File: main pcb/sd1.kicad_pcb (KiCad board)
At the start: 2 copper layers, 66.1 x 60 mm, 14 parts

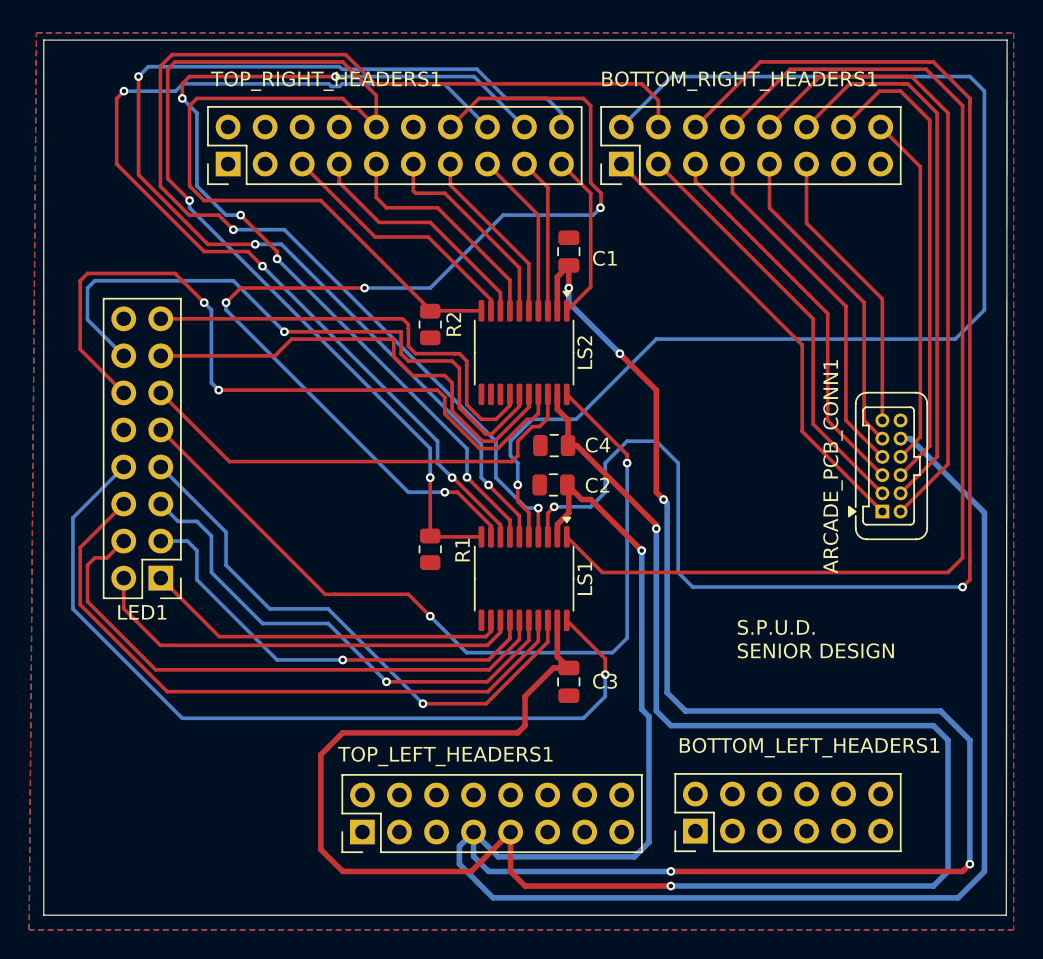
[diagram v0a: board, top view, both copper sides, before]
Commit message: updated main pcb with new connector
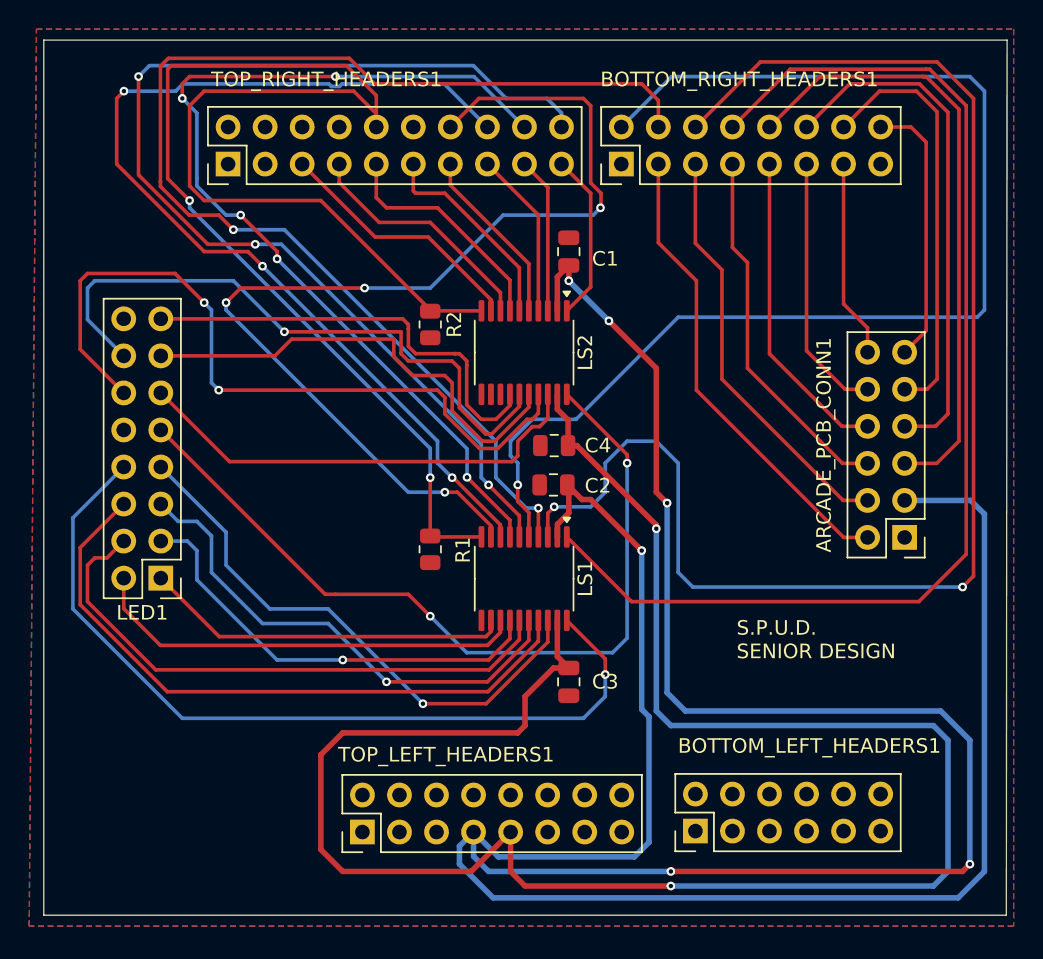
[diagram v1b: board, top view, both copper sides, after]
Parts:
- ARCADE_PCB_CONN1: footprint Connector_Harwin:Harwin_Gecko-G125-FVX1205L0X_2x06_P1.25mm_Vertical -> Connector_PinHeader_2.54mm:PinHeader_2x06_P2.54mm_Vertical
- moved ARCADE_PCB_CONN1 2.34 mm to (174.0, 109.1), turned to 180 degrees
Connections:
- ARCADE_PCB_CONN1 pad 1: ARC1 -> GND
- ARCADE_PCB_CONN1 pad 10: ARC10 -> ARC5
- ARCADE_PCB_CONN1 pad 11: 3.3V -> ARC10
- ARCADE_PCB_CONN1 pad 12: GND -> ARC6
- ARCADE_PCB_CONN1 pad 2: ARC2 -> ARC1
- ARCADE_PCB_CONN1 pad 3: ARC3 -> 3.3V
- ARCADE_PCB_CONN1 pad 4: ARC4 -> ARC2
- ARCADE_PCB_CONN1 pad 5: ARC5 -> ARC7
- ARCADE_PCB_CONN1 pad 6: ARC6 -> ARC3
- ARCADE_PCB_CONN1 pad 7: ARC7 -> ARC8
- ARCADE_PCB_CONN1 pad 8: ARC8 -> ARC4
- BOTTOM_RIGHT_HEADERS1 pad 1: ARC1 -> unconnected-(BOTTOM_RIGHT_HEADERS1-IO-Pad1)
- BOTTOM_RIGHT_HEADERS1 pad 11: ARC6 -> ARC5
- BOTTOM_RIGHT_HEADERS1 pad 13: unconnected-(BOTTOM_RIGHT_HEADERS1-IO-Pad13) -> ARC6
- BOTTOM_RIGHT_HEADERS1 pad 3: ARC2 -> ARC1
- BOTTOM_RIGHT_HEADERS1 pad 5: ARC3 -> ARC2
- BOTTOM_RIGHT_HEADERS1 pad 7: ARC4 -> ARC3
- BOTTOM_RIGHT_HEADERS1 pad 9: ARC5 -> ARC4
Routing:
- net ARC6: track 19.7 -> 13.6 mm
- net ARC10: track 24.3 -> 18.6 mm
- net ARC9: track 32.9 -> 28.9 mm
- net ARC5: track 22.0 -> 18.1 mm
- net ARC4: track 24.3 -> 21.8 mm
- net ARC8: track 38.1 -> 35.7 mm
- net 3.3V: track 219.5 -> 217.4 mm
- net DATA1: track 78.0 -> 80.0 mm
- net ARC3: track 26.6 -> 25.4 mm
- net ARC1: track 31.2 -> 32.5 mm
- net ARC7: track 43.4 -> 42.5 mm
- net OE: track 104.0 -> 104.7 mm

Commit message: update main pcb
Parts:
- LED1: value Conn_02x08_Top_Bottom -> Conn_02x08_Odd_Even
- moved LED1 16.0 mm to (120.5, 96.1), turned to 0 degrees
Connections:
- LED1 pad 10: GND -> A1
- LED1 pad 11: G1 -> A2
- LED1 pad 12: A4 -> A3
- LED1 pad 13: A1 -> Clock
- LED1 pad 14: A3 -> LATCH
- LED1 pad 15: LATCH -> BLANK
- LED1 pad 2: B0 -> G0
- LED1 pad 3: R1 -> B0
- LED1 pad 4: B1 -> GND
- LED1 pad 5: A0 -> R1
- LED1 pad 6: A2 -> G1
- LED1 pad 7: Clock -> B1
- LED1 pad 8: BLANK -> A4
- LED1 pad 9: G0 -> A0
- LS1 pad 12: R0 -> BLANK
- LS1 pad 13: B0 -> Clock
- LS1 pad 14: R1 -> A2
- LS1 pad 15: B1 -> A0
- LS1 pad 16: A0 -> B1
- LS1 pad 17: A2 -> R1
- LS1 pad 18: Clock -> B0
- LS1 pad 20: BLANK -> R0
- LS2 pad 14: LATCH -> G0
- LS2 pad 15: A3 -> G1
- LS2 pad 16: A1 -> A4
- LS2 pad 17: A4 -> A1
- LS2 pad 18: G1 -> A3
- LS2 pad 20: G0 -> LATCH
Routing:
- net R0: track 25.2 -> 70.5 mm, vias 0 -> 2
- net G0: track 57.1 -> 27.1 mm, vias 2 -> 1
- net B0: track 30.2 -> 59.8 mm, vias 0 -> 1
- net BLANK: track 57.7 -> 28.9 mm, vias 1 -> 2
- net R1: track 30.8 -> 54.9 mm, vias 1 -> 2
- net A4: track 51.4 -> 28.0 mm, vias 2 -> 1
- net LATCH: track 30.6 -> 53.2 mm, vias 0 -> 2
- net A3: track 43.9 -> 31.7 mm
- net A0: track 34.3 -> 46.5 mm, vias 1 -> 2
- net B1: track 39.4 -> 50.4 mm, vias 0 -> 1
- net G1: track 32.0 -> 26.6 mm, vias 0 -> 1
- net A1: track 32.3 -> 29.4 mm, vias 0 -> 1
- net A2: track 44.9 -> 42.6 mm, vias 0 -> 1
- net DATA7: track 70.0 -> 72.0 mm
- net OE: track 104.7 -> 106.4 mm, vias 2 -> 4
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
